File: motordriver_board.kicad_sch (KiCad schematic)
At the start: 70 parts, among them IC1 AZ1117CH-3.3TRG1, J1 Conn_01x05_Socket, J10 RJ45, J11 USB_C_Receptacle_USB2.0, J12 Conn_01x03_Socket, J13 Conn_02x07_Odd_Even, J14 RJ45, J15 Conn_01x02_Socket, J2 Conn_01x02, J3 Conn_01x02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

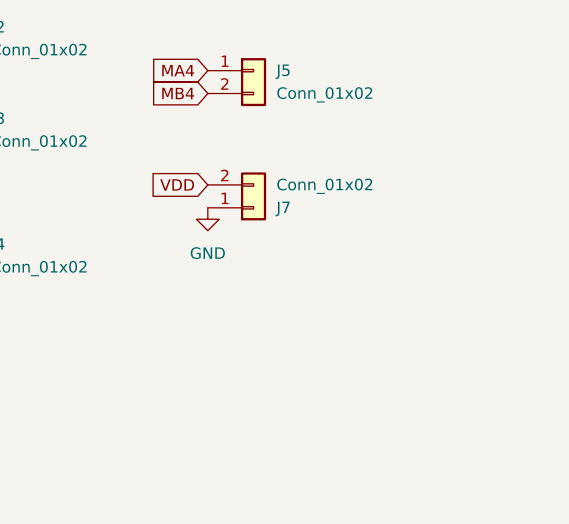
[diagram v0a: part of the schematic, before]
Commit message: 並列にXT60追加
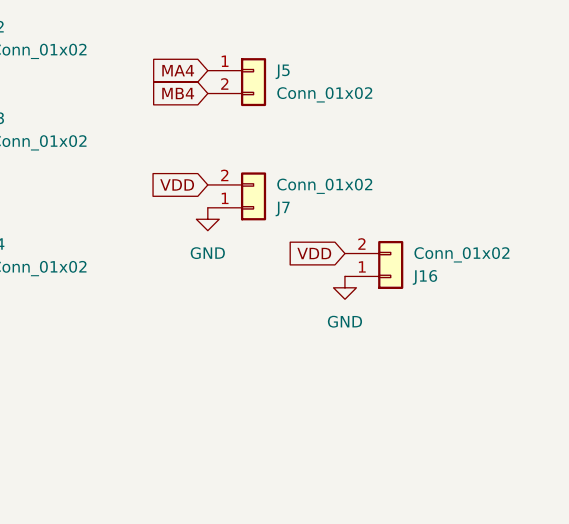
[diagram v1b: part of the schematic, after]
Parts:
- added J16: Conn_01x02, Connector_AMASS:AMASS_XT60PW-M_1x02_P7.20mm_Horizontal, symbol Connector_Generic:Conn_01x02
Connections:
- net GND: now also J16.1 (Pin_1)
- net VDD: now also J16.2 (Pin_2)
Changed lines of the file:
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@@
     )
   )
+  (global_label "VDD" (shape input) (at 267.97 162.56 180) (fields_autoplaced)
+    (effects (font (size 1.27 1.27)) (justify right))
+    (property "Intersheetrefs" "${INTERSHEET_REFS}" (at 261.3562 162.56 0)
+      (effects (font (size 1.27 1.27)) (justify right) hide)
+    )
+  )
   (global_label "CANL" (shape input) (at 57.404 83.058 0) (fields_autoplaced)
     (effects (font (size 1.27 1.27)) (justify left))
@@
     )
   )
+  (symbol (lib_id "power:GND") (at 267.97 165.1 0) (unit 1)
+    (in_bom yes) (on_board yes) (dnp no) (fields_autoplaced)
+    (property "Reference" "#PWR066" (at 267.97 171.45 0)
+      (effects (font (size 1.27 1.27)) hide)
+    )
+    (property "Value" "GND" (at 267.97 170.18 0)
+      (effects (font (size 1.27 1.27)))
+    )
+    (property "Footprint" "" (at 267.97 165.1 0)
+      (effects (font (size 1.27 1.27)) hide)
+    )
+    (property "Datasheet" "" (at 267.97 165.1 0)
+      (effects (font (size 1.27 1.27)) hide)
+    )
+    (pin "1")
+    (instances
+      (project "motordriver_board"
+        (path "/5aa24e62-4c81-4607-b371-076f7ad72490"
+          (reference "#PWR066") (unit 1)
+        )
+      )
+    )
+  )
   (symbol (lib_id "power:+3.3V") (at 65.786 114.808 0) (unit 1)
     (in_bom yes) (on_board yes) (dnp no)
@@
         )
       )
+    )
+  )
+  (symbol (lib_id "Connector_Generic:Conn_01x02") (at 273.05 165.1 0) (mirror x) (unit 1)
+    (in_bom yes) (on_board yes) (dnp no)
+    (property "Reference" "J16" (at 275.59 165.1 0)
+      (effects (font (size 1.27 1.27)) (justify left))
+    )
+    (property "Value" "Conn_01x02" (at 275.59 162.56 0)
+      (effects (font (size 1.27 1.27)) (justify left))
+    )
+    (property "Footprint" "Connector_AMASS:AMASS_XT60PW-M_1x02_P7.20mm_Horizontal" (at 273.05 165.1 0)
+      (effects (font (size 1.27 1.27)) hide)
+    )
+    (property "Datasheet" "~" (at 273.05 165.1 0)
+      (effects (font (size 1.27 1.27)) hide)
+    )
+    (pin "1")
+    (pin "2")
+    (instances
+      (project "motordriver_board"
+        (path "/5aa24e62-4c81-4607-b371-076f7ad72490"
+          (reference "J16") (unit 1)
+        )
+      )
